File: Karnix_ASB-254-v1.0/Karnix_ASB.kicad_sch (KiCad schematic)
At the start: 60 parts, among them SW1 SW_Push

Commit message: Remove rudimentary referencies to old projects
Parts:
- renumbered SW1 to SW2, SW1 to SW3, SW1 to SW4, XS3 to XS1, XS9 to XS10, XS9 to XS11, XS9 to XS3, XS9 to XS6, XS9 to XS7, XS9 to XS8
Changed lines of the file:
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@@
   (symbol (lib_id "Fabmicro:CONN_2Pins") (at 72.644 153.543 0) (unit 1)
     (in_bom yes) (on_board yes) (dnp no)
-    (property "Reference" "XS9" (at 76.962 152.273 0)
+    (property "Reference" "XS7" (at 76.962 152.273 0)
       (effects (font (size 1.27 1.27)))
     )
@@
     (pin "2")
     (instances
-      (project "SIP_HomePhone"
-        (path "/1f1efc58-1a2e-4658-b2ac-cf03134c8a7b/00000000-0000-0000-0000-00005ddd780c"
-          (reference "XS9") (unit 1)
-        )
-      )
-      (project "RanetkaPC_SBC"
-        (path "/ec71f5a1-9121-4fc3-8b2f-749f8a7afeed/00000000-0000-0000-0000-00005e82d990"
-          (reference "XS2") (unit 1)
-        )
-      )
       (project "Karnix_ASB"
         (path "/fe37e245-9527-4c72-91fc-09b617a42f73"
@@
   (symbol (lib_id "Fabmicro:CONN_2Pins") (at 73.279 202.565 0) (unit 1)
     (in_bom yes) (on_board yes) (dnp no)
-    (property "Reference" "XS9" (at 77.597 201.295 0)
+    (property "Reference" "XS10" (at 77.597 201.295 0)
       (effects (font (size 1.27 1.27)))
     )
@@
     (pin "2")
     (instances
-      (project "SIP_HomePhone"
-        (path "/1f1efc58-1a2e-4658-b2ac-cf03134c8a7b/00000000-0000-0000-0000-00005ddd780c"
-          (reference "XS9") (unit 1)
-        )
-      )
-      (project "RanetkaPC_SBC"
-        (path "/ec71f5a1-9121-4fc3-8b2f-749f8a7afeed/00000000-0000-0000-0000-00005e82d990"
-          (reference "XS2") (unit 1)
-        )
-      )
       (project "Karnix_ASB"
         (path "/fe37e245-9527-4c72-91fc-09b617a42f73"
@@
   (symbol (lib_id "Fabmicro:CONN_2Pins") (at 72.771 166.624 0) (unit 1)
     (in_bom yes) (on_board yes) (dnp no)
-    (property "Reference" "XS9" (at 77.089 165.354 0)
+    (property "Reference" "XS8" (at 77.089 165.354 0)
       (effects (font (size 1.27 1.27)))
     )
@@
     (pin "2")
     (instances
-      (project "SIP_HomePhone"
-        (path "/1f1efc58-1a2e-4658-b2ac-cf03134c8a7b/00000000-0000-0000-0000-00005ddd780c"
-          (reference "XS9") (unit 1)
-        )
-      )
-      (project "RanetkaPC_SBC"
-        (path "/ec71f5a1-9121-4fc3-8b2f-749f8a7afeed/00000000-0000-0000-0000-00005e82d990"
-          (reference "XS2") (unit 1)
-        )
-      )
       (project "Karnix_ASB"
         (path "/fe37e245-9527-4c72-91fc-09b617a42f73"
@@
   (symbol (lib_id "Switch:SW_Push") (at 147.32 157.607 0) (unit 1)
     (in_bom yes) (on_board yes) (dnp no)
-    (property "Reference" "SW1" (at 135.128 156.2927 0)
+    (property "Reference" "SW3" (at 135.128 156.2927 0)
       (effects (font (size 1.27 1.27)))
     )
@@
     (pin "2")
     (instances
-      (project "OrangeCrab"
-        (path "/4e8f832c-e89e-43c4-aa3b-05785457571c/00000000-0000-0000-0000-00005abc9a87"
-          (reference "SW1") (unit 1)
-        )
-      )
       (project "Karnix_ASB"
         (path "/fe37e245-9527-4c72-91fc-09b617a42f73"
@@
   (symbol (lib_id "Fabmicro:CONN_2Pins") (at 72.771 119.253 0) (unit 1)
     (in_bom yes) (on_board yes) (dnp no)
-    (property "Reference" "XS9" (at 77.089 117.983 0)
+    (property "Reference" "XS3" (at 77.089 117.983 0)
       (effects (font (size 1.27 1.27)))
     )
@@
     (pin "2")
     (instances
-      (project "SIP_HomePhone"
-        (path "/1f1efc58-1a2e-4658-b2ac-cf03134c8a7b/00000000-0000-0000-0000-00005ddd780c"
-          (reference "XS9") (unit 1)
-        )
-      )
-      (project "RanetkaPC_SBC"
-        (path "/ec71f5a1-9121-4fc3-8b2f-749f8a7afeed/00000000-0000-0000-0000-00005e82d990"
-          (reference "XS2") (unit 1)
-        )
-      )
       (project "Karnix_ASB"
         (path "/fe37e245-9527-4c72-91fc-09b617a42f73"
@@
   (symbol (lib_id "Fabmicro:CONN_2Pins") (at 72.644 140.335 0) (unit 1)
     (in_bom yes) (on_board yes) (dnp no)
-    (property "Reference" "XS9" (at 76.962 139.065 0)
+    (property "Reference" "XS6" (at 76.962 139.065 0)
       (effects (font (size 1.27 1.27)))
     )
@@
     (pin "2")
     (instances
-      (project "SIP_HomePhone"
-        (path "/1f1efc58-1a2e-4658-b2ac-cf03134c8a7b/00000000-0000-0000-0000-00005ddd780c"
-          (reference "XS9") (unit 1)
-        )
-      )
-      (project "RanetkaPC_SBC"
-        (path "/ec71f5a1-9121-4fc3-8b2f-749f8a7afeed/00000000-0000-0000-0000-00005e82d990"
-          (reference "XS2") (unit 1)
-        )
-      )
       (project "Karnix_ASB"
         (path "/fe37e245-9527-4c72-91fc-09b617a42f73"
@@
   (symbol (lib_id "Fabmicro:CONN_2Pins") (at 72.898 215.773 0) (unit 1)
     (in_bom yes) (on_board yes) (dnp no)
-    (property "Reference" "XS9" (at 77.216 214.503 0)
+    (property "Reference" "XS11" (at 77.216 214.503 0)
       (effects (font (size 1.27 1.27)))
     )
@@
     (pin "2")
     (instances
-      (project "SIP_HomePhone"
-        (path "/1f1efc58-1a2e-4658-b2ac-cf03134c8a7b/00000000-0000-0000-0000-00005ddd780c"
-          (reference "XS9") (unit 1)
-        )
-      )
-      (project "RanetkaPC_SBC"
-        (path "/ec71f5a1-9121-4fc3-8b2f-749f8a7afeed/00000000-0000-0000-0000-00005e82d990"
-          (reference "XS2") (unit 1)
-        )
-      )
       (project "Karnix_ASB"
         (path "/fe37e245-9527-4c72-91fc-09b617a42f73"
@@
   (symbol (lib_id "Fabmicro:CONN_2Pins") (at 72.136 92.075 0) (unit 1)
     (in_bom yes) (on_board yes) (dnp no)
-    (property "Reference" "XS3" (at 75.692 90.678 0)
+    (property "Reference" "XS1" (at 75.692 90.678 0)
       (effects (font (size 1.27 1.27)))
     )
@@
     (pin "2")
     (instances
-      (project "RanetkaPC_SBC"
-        (path "/ec71f5a1-9121-4fc3-8b2f-749f8a7afeed/00000000-0000-0000-0000-00005ddd7771"
-          (reference "XS3") (unit 1)
-        )
-      )
       (project "Karnix_ASB"
         (path "/fe37e245-9527-4c72-91fc-09b617a42f73"
@@
   (symbol (lib_id "Switch:SW_Push") (at 147.32 164.719 0) (unit 1)
     (in_bom yes) (on_board yes) (dnp no)
-    (property "Reference" "SW1" (at 135.128 163.4047 0)
+    (property "Reference" "SW4" (at 135.128 163.4047 0)
       (effects (font (size 1.27 1.27)))
     )
@@
     (pin "2")
     (instances
-      (project "OrangeCrab"
-        (path "/4e8f832c-e89e-43c4-aa3b-05785457571c/00000000-0000-0000-0000-00005abc9a87"
-          (reference "SW1") (unit 1)
-        )
-      )
       (project "Karnix_ASB"
         (path "/fe37e245-9527-4c72-91fc-09b617a42f73"
@@
     (pin "2")
     (instances
-      (project "SIP_HomePhone"
-        (path "/1f1efc58-1a2e-4658-b2ac-cf03134c8a7b/00000000-0000-0000-0000-00005ddd780c"
-          (reference "XS9") (unit 1)
-        )
-      )
-      (project "RanetkaPC_SBC"
-        (path "/ec71f5a1-9121-4fc3-8b2f-749f8a7afeed/00000000-0000-0000-0000-00005e82d990"
-          (reference "XS2") (unit 1)
-        )
-      )
       (project "Karnix_ASB"
         (path "/fe37e245-9527-4c72-91fc-09b617a42f73"
@@
     (pin "2")
     (instances
-      (project "OrangeCrab"
-        (path "/4e8f832c-e89e-43c4-aa3b-05785457571c/00000000-0000-0000-0000-00005abc9a87"
-          (reference "SW1") (unit 1)
-        )
-      )
       (project "Karnix_ASB"
         (path "/fe37e245-9527-4c72-91fc-09b617a42f73"
@@
   (symbol (lib_id "power:+5V") (at 260.8904 82.4061 0) (unit 1)
     (in_bom yes) (on_board yes) (dnp no) (fields_autoplaced)
-    (property "Reference" "#PWR023" (at 260.8904 86.2161 0)
+    (property "Reference" "#PWR0146" (at 260.8904 86.2161 0)
       (effects (font (size 1.27 1.27)) hide)
     )
@@
     (pin "1")
     (instances
-      (project "Analog_16_8"
-        (path "/121afcc6-94a7-450a-a879-4c3eaa09954e/00000000-0000-0000-0000-00005ddd7771"
-          (reference "#PWR023") (unit 1)
-        )
-      )
-      (project "Power"
-        (path "/ecd93358-d394-4c7e-b496-f2c7d3a08d3b"
-          (reference "#PWR023") (unit 1)
-        )
-      )
       (project "Karnix_ASB"
         (path "/fe37e245-9527-4c72-91fc-09b617a42f73/00000000-0000-0000-0000-0000602e0fd3"
@@
   (symbol (lib_id "Switch:SW_Push") (at 147.32 150.241 0) (unit 1)
     (in_bom yes) (on_board yes) (dnp no)
-    (property "Reference" "SW1" (at 135.128 148.9267 0)
+    (property "Reference" "SW2" (at 135.128 148.9267 0)
       (effects (font (size 1.27 1.27)))
     )
@@
     (pin "2")
     (instances
-      (project "OrangeCrab"
-        (path "/4e8f832c-e89e-43c4-aa3b-05785457571c/00000000-0000-0000-0000-00005abc9a87"
-          (reference "SW1") (unit 1)
-        )
-      )
-      (project "Karnix_ASB"
-        (path "/fe37e245-9527-4c72-91fc-09b617a42f73"
+      (project "Karnix_ASB"
+        (path "/fe37e245-9527-4c72-91fc-09b617a42f73"

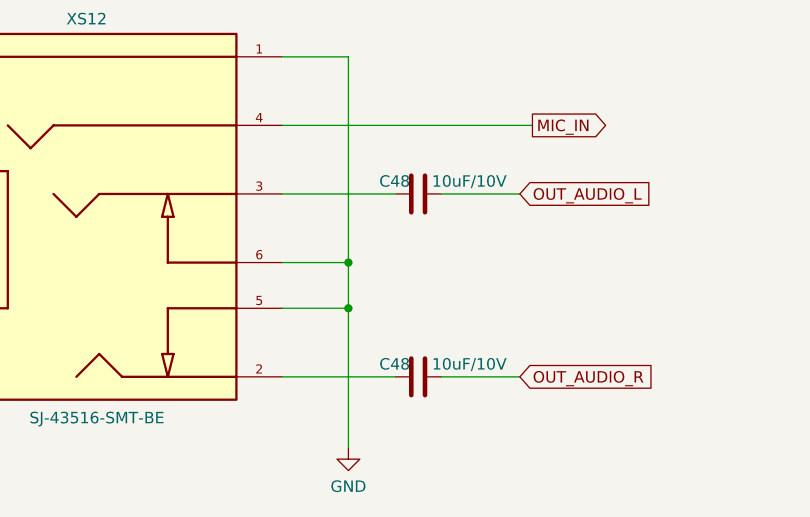
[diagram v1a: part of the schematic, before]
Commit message: Route JTAG and FPGA config. Fanout GPIO.
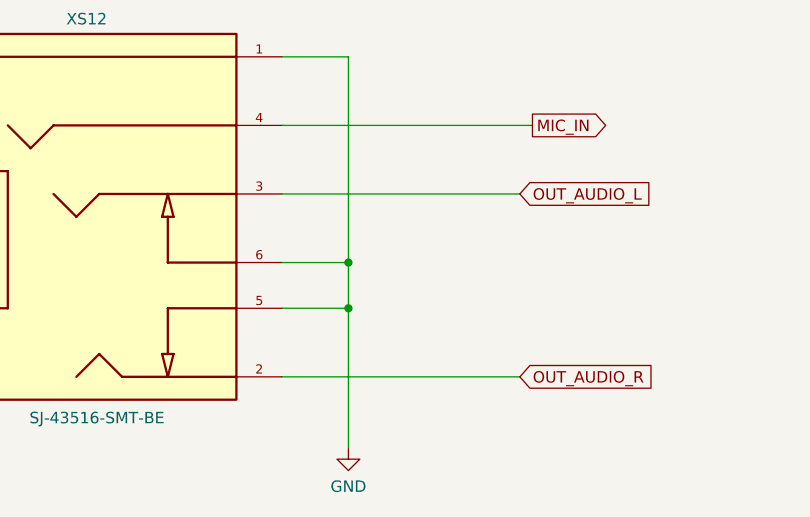
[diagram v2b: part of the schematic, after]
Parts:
- removed C48 (x2): 10uF/10V, Capacitor_SMD:C_0603_1608Metric, symbol Fabmicro:CapacitorUnpolarized
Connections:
- net OUT_AUDIO_L: now also XS12.3
- net OUT_AUDIO_R: now also XS12.2
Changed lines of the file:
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@@
     (stroke (width 0) (type default))
   )
-  (wire (pts (xy 170.434 210.058) (xy 157.861 210.058))
+  (wire (pts (xy 157.861 210.058) (xy 184.277 210.058))
     (stroke (width 0) (type default))
   )
@@
     (stroke (width 0) (type default))
   )
-  (wire (pts (xy 170.434 230.378) (xy 157.861 230.378))
-    (stroke (width 0) (type default))
-  )
   (wire (pts (xy 266.1482 107.7807) (xy 255.925 107.7807))
     (stroke (width 0) (type default))
@@
     (stroke (width 0) (type default))
   )
+  (wire (pts (xy 157.861 230.378) (xy 184.277 230.378))
+    (stroke (width 0) (type default))
+  )
   (wire (pts (xy 87.249 94.615) (xy 84.836 94.615))
     (stroke (width 0) (type default))
@@
     (stroke (width 0) (type default))
   )
-  (wire (pts (xy 184.277 210.058) (xy 175.514 210.058))
-    (stroke (width 0) (type default))
-  )
   (wire (pts (xy 162.687 92.329) (xy 162.687 99.949))
     (stroke (width 0) (type default))
@@
   )
   (wire (pts (xy 153.035 150.241) (xy 152.4 150.241))
-    (stroke (width 0) (type default))
-  )
-  (wire (pts (xy 184.277 230.378) (xy 175.514 230.378))
     (stroke (width 0) (type default))
   )
@@
     )
   )
-  (symbol (lib_id "Fabmicro:CapacitorUnpolarized") (at 172.974 210.058 0) (mirror x) (unit 1)
-    (in_bom yes) (on_board yes) (dnp no)
-    (property "Reference" "C48" (at 168.656 208.661 0)
-      (effects (font (size 1.27 1.27)) (justify left))
-    )
-    (property "Value" "10uF/10V" (at 174.498 208.661 0)
-      (effects (font (size 1.27 1.27)) (justify left))
-    )
-    (property "Footprint" "Capacitor_SMD:C_0603_1608Metric" (at 176.784 211.0232 90)
-      (effects (font (size 1.27 1.27)) hide)
-    )
-    (property "Datasheet" "~" (at 172.974 210.058 90)
-      (effects (font (size 1.27 1.27)) hide)
-    )
-    (property "Mfr. Part Number" "GRM188R61A106KE69D" (at 172.974 210.058 0)
-      (effects (font (size 1.27 1.27)) hide)
-    )
-    (property "Supplier" "Fabmicro" (at 172.974 210.058 0)
-      (effects (font (size 1.27 1.27)) hide)
-    )
-    (pin "1")
-    (pin "2")
-    (instances
-      (project "Karnix_ASB"
-        (path "/fe37e245-9527-4c72-91fc-09b617a42f73/00000000-0000-0000-0000-0000602e11fa"
-          (reference "C48") (unit 1)
-        )
-        (path "/fe37e245-9527-4c72-91fc-09b617a42f73"
-          (reference "C82") (unit 1)
-        )
-      )
-    )
-  )
   (symbol (lib_id "power:GND") (at 162.687 121.92 0) (mirror y) (unit 1)
     (in_bom yes) (on_board yes) (dnp no)
@@
         )
       )
-    )
-  )
-  (symbol (lib_id "Fabmicro:CapacitorUnpolarized") (at 172.974 230.378 0) (mirror x) (unit 1)
-    (in_bom yes) (on_board yes) (dnp no)
-    (property "Reference" "C48" (at 168.656 228.981 0)
-      (effects (font (size 1.27 1.27)) (justify left))
-    )
-    (property "Value" "10uF/10V" (at 174.498 228.981 0)
-      (effects (font (size 1.27 1.27)) (justify left))
-    )
-    (property "Footprint" "Capacitor_SMD:C_0603_1608Metric" (at 176.784 231.3432 90)
-      (effects (font (size 1.27 1.27)) hide)
-    )
-    (property "Datasheet" "~" (at 172.974 230.378 90)
-      (effects (font (size 1.27 1.27)) hide)
-    )
-    (property "Mfr. Part Number" "GRM188R61A106KE69D" (at 172.974 230.378 0)
-      (effects (font (size 1.27 1.27)) hide)
-    )
-    (property "Supplier" "Fabmicro" (at 172.974 230.378 0)
-      (effects (font (size 1.27 1.27)) hide)
-    )
-    (pin "1")
-    (pin "2")
-    (instances
-      (project "Karnix_ASB"
-        (path "/fe37e245-9527-4c72-91fc-09b617a42f73/00000000-0000-0000-0000-0000602e11fa"
-          (reference "C48") (unit 1)
-        )
-        (path "/fe37e245-9527-4c72-91fc-09b617a42f73"
-          (reference "C83") (unit 1)
-        )
-      )
